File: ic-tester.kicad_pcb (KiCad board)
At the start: 2 copper layers, 91.4 x 68.6 mm, 15 parts, among them IC1 MCP23017-E_SP, IC2 MCP23017-E_SP, IC3 MCP23017-E_SP, SW1 SW_SPST

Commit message: For production.
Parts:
- added J1: Conn_01x04, Connector_PinHeader_2.54mm:PinHeader_1x04_P2.54mm_Vertical, F.Cu at (40.0, 78.1)
- moved J_GPIO1 14.3 mm to (40.0, 75.6)
- moved SW1 7.62 mm to (40.0, 32.4)
- moved R1 0.64 mm to (109.2, 47.6)
- moved R2 0.64 mm to (109.2, 54.0)
- moved R3 0.64 mm to (109.2, 67.9)
- moved R4 0.64 mm to (109.2, 81.9)
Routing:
- net GND: track 238.2 -> 288.5 mm
- net VDD: track 195.5 -> 174.8 mm
- net Net-(IC3-Pad24): track 110.7 -> 123.8 mm
- net /GPIO2: track 13.4 -> 21.4 mm
- net /GPIO1: track 6.02 -> 13.8 mm
- net /GPIO3: track 14.1 -> 21.4 mm
- net /GPIO4: track 13.4 -> 20.4 mm
- net /LED_OK: track 72.3 -> 71.3 mm
- net /LED_RDY: track 82.4 -> 81.7 mm
- net Net-(D4-Pad2): track 8.67 -> 8.04 mm
- net Net-(D3-Pad2): track 8.67 -> 8.04 mm
- net Net-(D2-Pad2): track 8.67 -> 8.04 mm
- net Net-(D1-Pad2): track 9.72 -> 9.09 mm
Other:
- board text added: "${DOC_COMPANY}"
- board text added: "${DOC_TITLE}"
- board text added: "GND"
- board text added: "Revision ${REV} / ${DATE}"
- board text removed: "%R"
- board text removed: "Raspberry PI IC Tester"
- board text removed: "https://github.com/madworx"

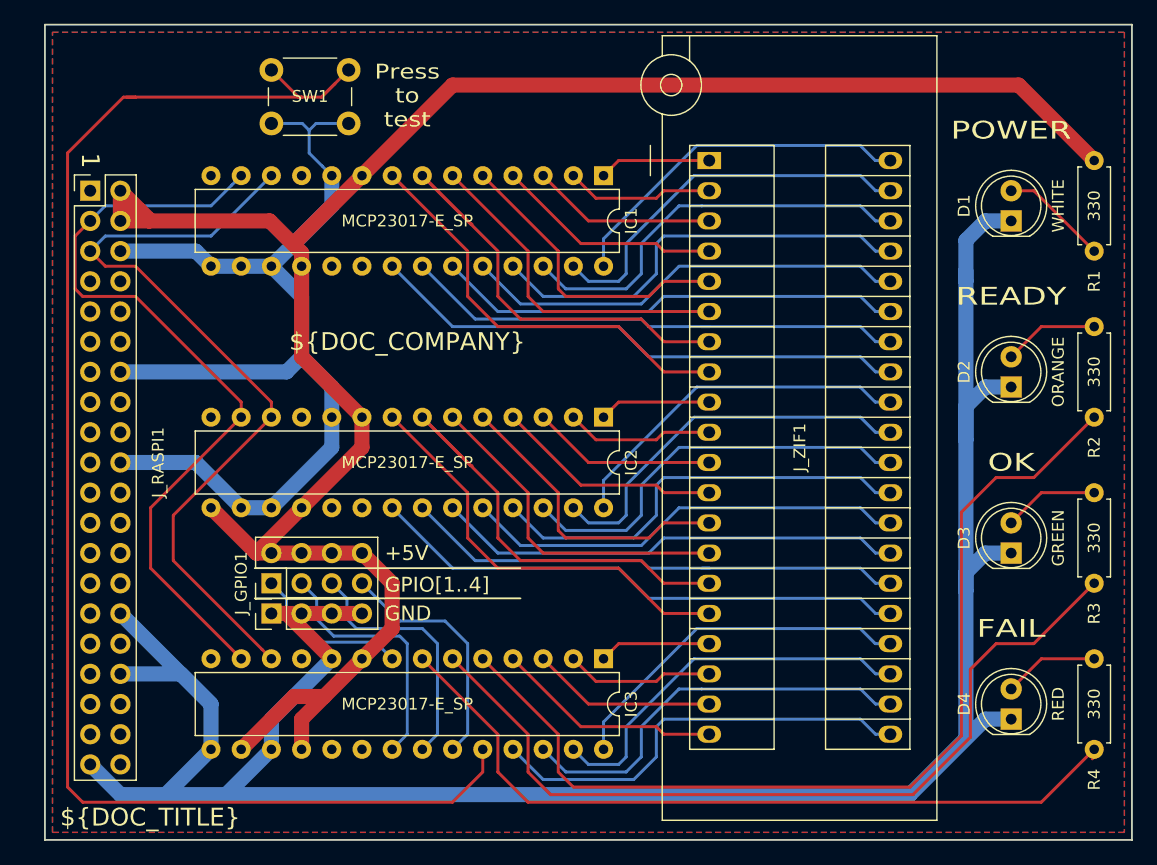
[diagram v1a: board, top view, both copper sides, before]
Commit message: Added 3D models for correctly coloured LEDs, as well as ZIF-socket. Reduced reundandant tracks.
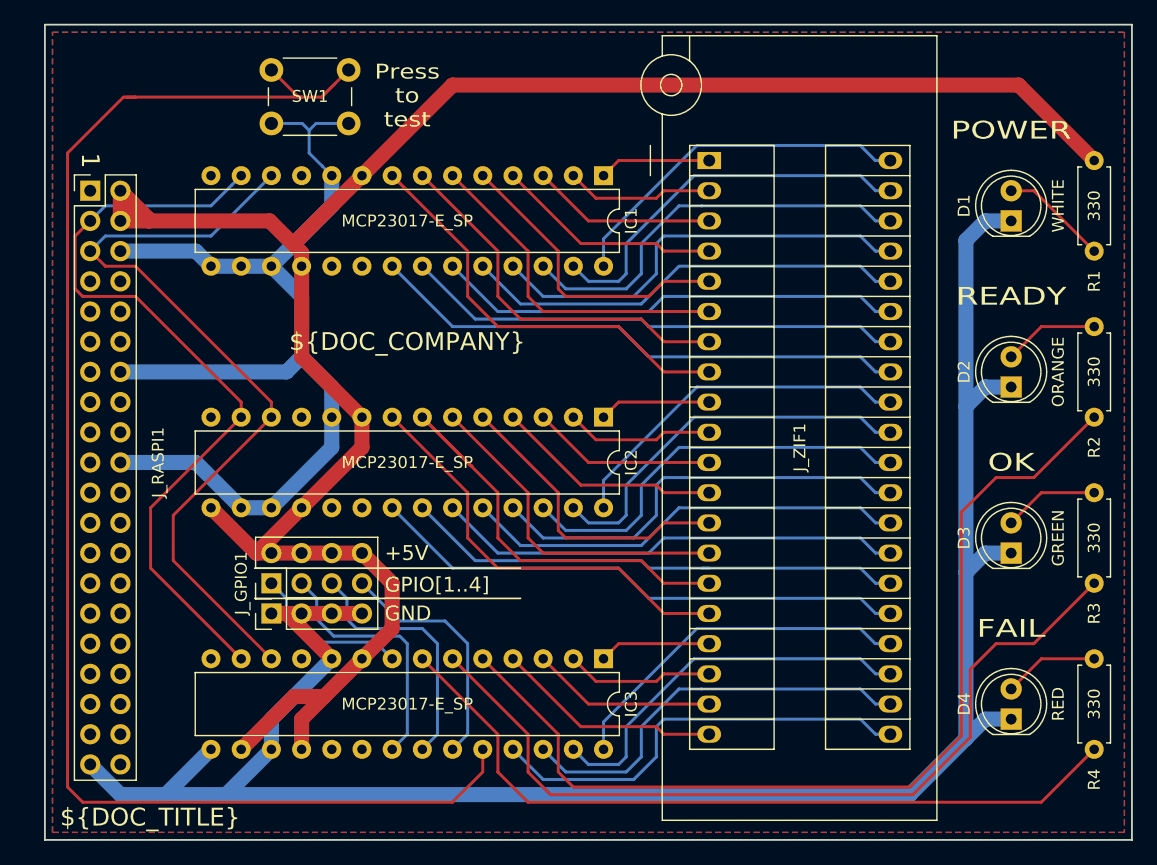
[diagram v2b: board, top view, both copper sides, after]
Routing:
- net GND: track 288.5 -> 260.4 mm
- net /ZIF07: track 38.0 -> 32.1 mm
- net /LED_FAIL: track 66.3 -> 65.2 mm
